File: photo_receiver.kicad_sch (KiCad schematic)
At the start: 7 parts

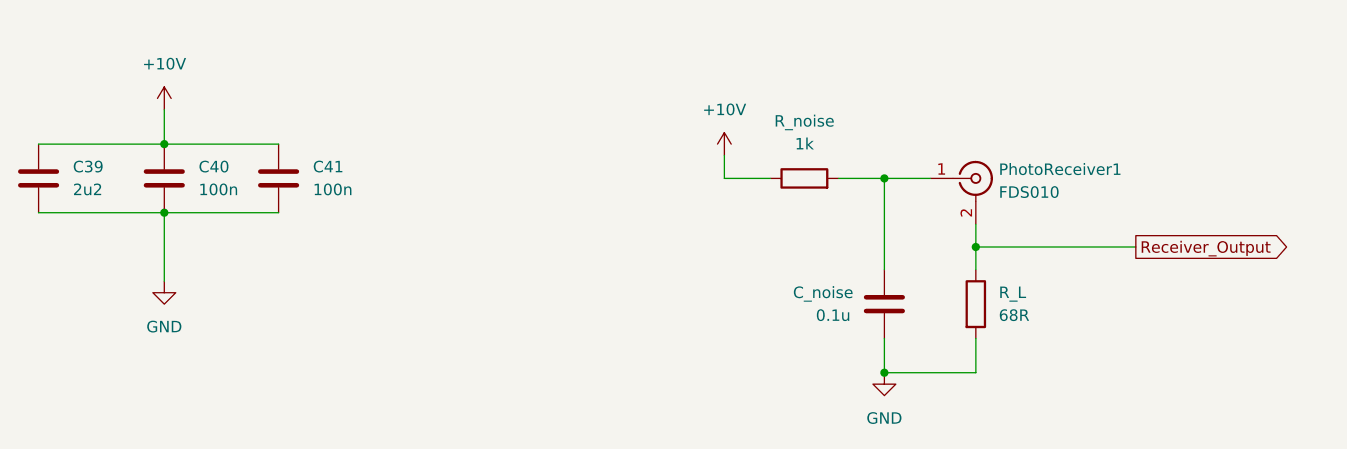
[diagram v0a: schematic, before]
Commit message: Resistor and cap footprints (except the ones the store cupboard doesn't have)
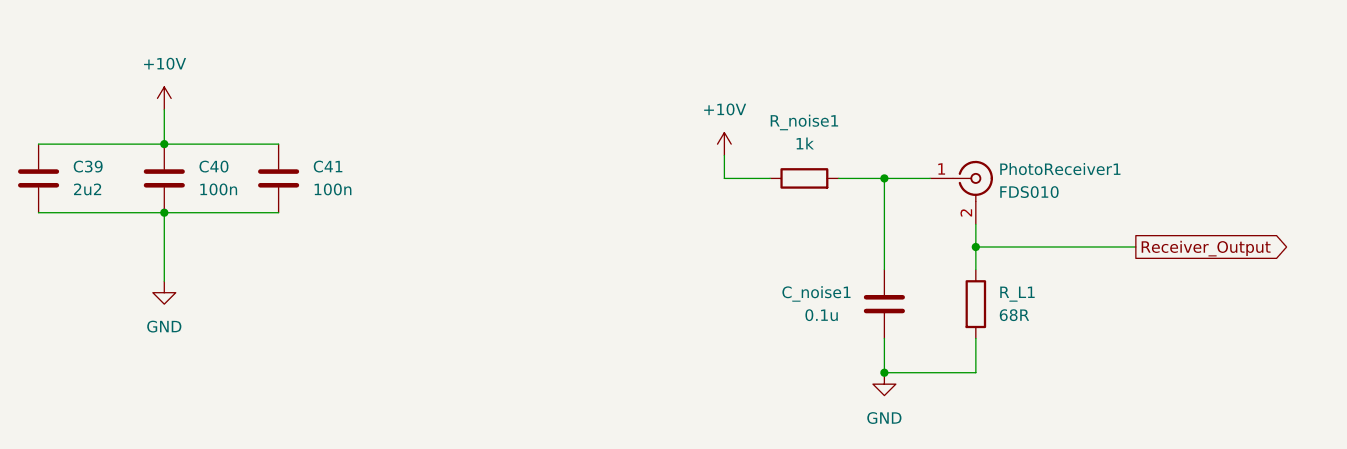
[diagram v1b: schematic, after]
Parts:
- C39: footprint (none) -> Capacitor_Tantalum_SMD:CP_EIA-3528-15_AVX-H_Pad1.50x2.35mm_HandSolder
- C40, C41: footprint (none) -> Capacitor_SMD:C_0805_2012Metric_Pad1.18x1.45mm_HandSolder
- C_noise1: renamed from C_noise; footprint (none) -> Capacitor_SMD:C_0805_2012Metric_Pad1.18x1.45mm_HandSolder
- R_L1: renamed from R_L; footprint (none) -> Resistor_SMD:R_0805_2012Metric_Pad1.20x1.40mm_HandSolder
- R_noise1: renamed from R_noise; footprint (none) -> Resistor_SMD:R_0805_2012Metric_Pad1.20x1.40mm_HandSolder
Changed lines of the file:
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@@
   (symbol (lib_id "Device:R") (at 123.19 91.44 90) (unit 1)
     (in_bom yes) (on_board yes) (fields_autoplaced)
-    (property "Reference" "R_noise" (id 0) (at 123.19 85.09 90))
+    (property "Reference" "R_noise1" (id 0) (at 123.19 85.09 90))
     (property "Value" "1k" (id 1) (at 123.19 87.63 90))
-    (property "Footprint" "" (id 2) (at 123.19 93.218 90)
+    (property "Footprint" "Resistor_SMD:R_0805_2012Metric_Pad1.20x1.40mm_HandSolder" (id 2) (at 123.19 93.218 90)
       (effects (font (size 1.27 1.27)) hide)
     )
@@
   (symbol (lib_id "Device:R") (at 142.24 105.41 0) (unit 1)
     (in_bom yes) (on_board yes) (fields_autoplaced)
-    (property "Reference" "R_L" (id 0) (at 144.78 104.1399 0)
+    (property "Reference" "R_L1" (id 0) (at 144.78 104.1399 0)
       (effects (font (size 1.27 1.27)) (justify left))
     )
@@
       (effects (font (size 1.27 1.27)) (justify left))
     )
-    (property "Footprint" "" (id 2) (at 140.462 105.41 90)
+    (property "Footprint" "Resistor_SMD:R_0805_2012Metric_Pad1.20x1.40mm_HandSolder" (id 2) (at 140.462 105.41 90)
       (effects (font (size 1.27 1.27)) hide)
     )
@@
       (effects (font (size 1.27 1.27)) (justify left))
     )
-    (property "Footprint" "" (id 2) (at 65.7352 95.25 0)
+    (property "Footprint" "Capacitor_SMD:C_0805_2012Metric_Pad1.18x1.45mm_HandSolder" (id 2) (at 65.7352 95.25 0)
       (effects (font (size 1.27 1.27)) hide)
     )
@@
   (symbol (lib_id "Device:C") (at 132.08 105.41 0) (unit 1)
     (in_bom yes) (on_board yes)
-    (property "Reference" "C_noise" (id 0) (at 121.92 104.14 0)
+    (property "Reference" "C_noise1" (id 0) (at 120.65 104.14 0)
       (effects (font (size 1.27 1.27)) (justify left))
     )
-    (property "Value" "0.1u" (id 1) (at 124.46 106.68 0)
+    (property "Value" "0.1u" (id 1) (at 123.19 106.68 0)
       (effects (font (size 1.27 1.27)) (justify left))
     )
-    (property "Footprint" "" (id 2) (at 133.0452 109.22 0)
+    (property "Footprint" "Capacitor_SMD:C_0805_2012Metric_Pad1.18x1.45mm_HandSolder" (id 2) (at 133.0452 109.22 0)
       (effects (font (size 1.27 1.27)) hide)
     )
@@
   (symbol (lib_id "power:GND") (at 132.08 113.03 0) (unit 1)
     (in_bom yes) (on_board yes) (fields_autoplaced)
-    (property "Reference" "#PWR?" (id 0) (at 132.08 119.38 0)
+    (property "Reference" "#PWR0108" (id 0) (at 132.08 119.38 0)
       (effects (font (size 1.27 1.27)) hide)
     )
@@
   (symbol (lib_id "power:+10V") (at 52.07 83.82 0) (unit 1)
     (in_bom yes) (on_board yes) (fields_autoplaced)
-    (property "Reference" "#PWR?" (id 0) (at 52.07 87.63 0)
+    (property "Reference" "#PWR0106" (id 0) (at 52.07 87.63 0)
       (effects (font (size 1.27 1.27)) hide)
     )
@@
       (effects (font (size 1.27 1.27)) (justify left))
     )
-    (property "Footprint" "" (id 2) (at 53.0352 95.25 0)
+    (property "Footprint" "Capacitor_SMD:C_0805_2012Metric_Pad1.18x1.45mm_HandSolder" (id 2) (at 53.0352 95.25 0)
       (effects (font (size 1.27 1.27)) hide)
     )
@@
   (symbol (lib_id "power:+10V") (at 114.3 88.9 0) (unit 1)
     (in_bom yes) (on_board yes) (fields_autoplaced)
-    (property "Reference" "#PWR?" (id 0) (at 114.3 92.71 0)
+    (property "Reference" "#PWR0107" (id 0) (at 114.3 92.71 0)
       (effects (font (size 1.27 1.27)) hide)
     )
@@
       (effects (font (size 1.27 1.27)) (justify left))
     )
-    (property "Footprint" "" (id 2) (at 39.0652 95.25 0)
+    (property "Footprint" "Capacitor_Tantalum_SMD:CP_EIA-3528-15_AVX-H_Pad1.50x2.35mm_HandSolder" (id 2) (at 39.0652 95.25 0)
       (effects (font (size 1.27 1.27)) hide)
     )

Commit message: added most of the sourcing info
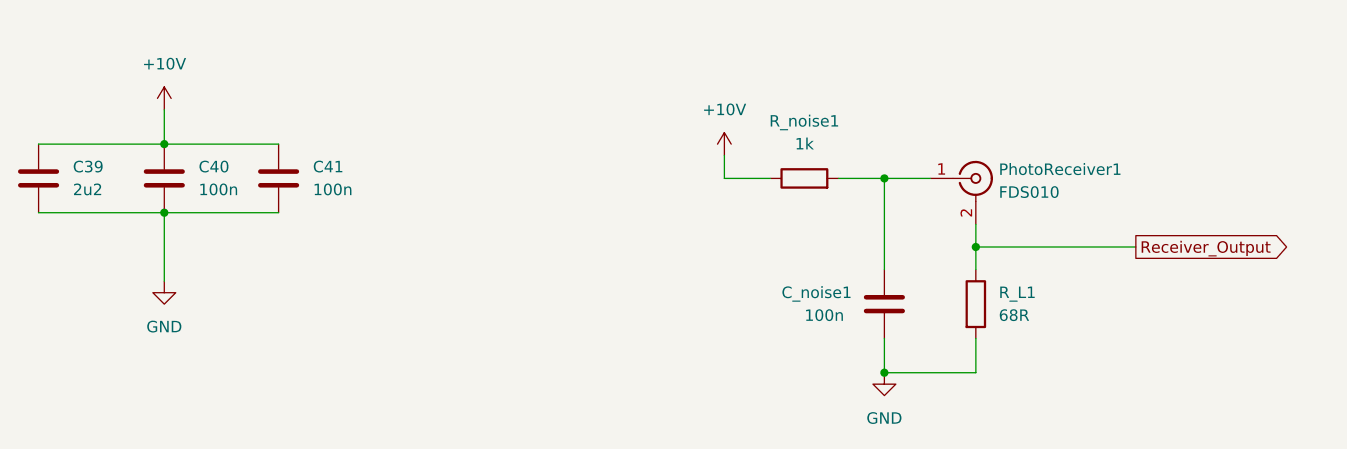
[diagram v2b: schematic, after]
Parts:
- C39, C40, C41, R_L1, R_noise1: Source (none) -> L3 store
- C_noise1: value 0.1u -> 100n; Source (none) -> L3 store
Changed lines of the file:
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@@
+      (effects (font (size 1.27 1.27)) hide)
+    )
+    (property "Source" "L3 store" (id 4) (at 123.19 91.44 0)
       (effects (font (size 1.27 1.27)) hide)
     )
@@
       (effects (font (size 1.27 1.27)) hide)
     )
+    (property "Source" "L3 store" (id 4) (at 142.24 105.41 0)
+      (effects (font (size 1.27 1.27)) hide)
+    )
     (pin "1")
     (pin "2")
@@
       (effects (font (size 1.27 1.27)) hide)
     )
+    (property "Source" "L3 store" (id 4) (at 64.77 91.44 0)
+      (effects (font (size 1.27 1.27)) hide)
+    )
     (pin "1")
     (pin "2")
@@
       (effects (font (size 1.27 1.27)) (justify left))
     )
-    (property "Value" "0.1u" (id 1) (at 123.19 106.68 0)
+    (property "Value" "100n" (id 1) (at 123.19 106.68 0)
       (effects (font (size 1.27 1.27)) (justify left))
     )
@@
     )
     (property "Datasheet" "~" (id 3) (at 132.08 105.41 0)
+      (effects (font (size 1.27 1.27)) hide)
+    )
+    (property "Source" "L3 store" (id 4) (at 132.08 105.41 0)
       (effects (font (size 1.27 1.27)) hide)
     )
@@
       (effects (font (size 1.27 1.27)) hide)
     )
+    (property "Source" "L3 store" (id 4) (at 52.07 91.44 0)
+      (effects (font (size 1.27 1.27)) hide)
+    )
     (pin "1")
     (pin "2")
@@
       (effects (font (size 1.27 1.27)) hide)
     )
+    (property "Source" "L3 store" (id 4) (at 38.1 91.44 0)
+      (effects (font (size 1.27 1.27)) hide)
+    )

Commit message: solved power drc problems
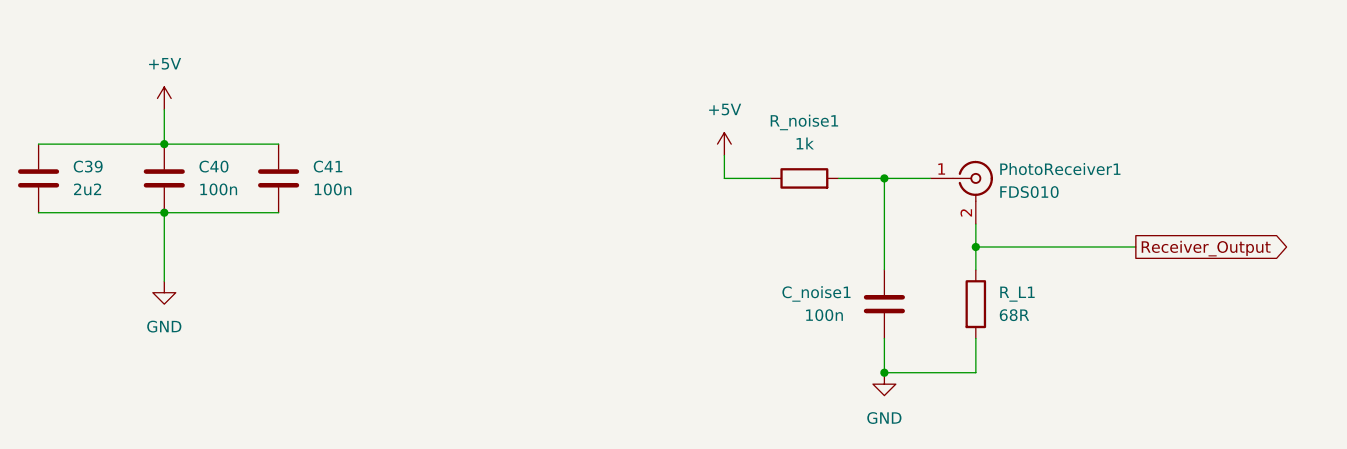
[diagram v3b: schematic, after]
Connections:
- net +10V renamed +5V
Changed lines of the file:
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@@
     (pin "2")
+  )
+  (symbol (lib_id "power:+5V") (at 114.3 88.9 0) (unit 1)
+    (in_bom yes) (on_board yes) (fields_autoplaced)
+    (property "Reference" "#PWR0107" (id 0) (at 114.3 92.71 0)
+      (effects (font (size 1.27 1.27)) hide)
+    )
+    (property "Value" "+5V" (id 1) (at 114.3 83.82 0))
+    (property "Footprint" "" (id 2) (at 114.3 88.9 0)
+      (effects (font (size 1.27 1.27)) hide)
+    )
+    (property "Datasheet" "" (id 3) (at 114.3 88.9 0)
+      (effects (font (size 1.27 1.27)) hide)
+    )
+    (pin "1")
   )
   (symbol (lib_id "Device:C") (at 132.08 105.41 0) (unit 1)
@@
     (pin "1")
   )
-  (symbol (lib_id "power:+10V") (at 52.07 83.82 0) (unit 1)
-    (in_bom yes) (on_board yes) (fields_autoplaced)
-    (property "Reference" "#PWR0106" (id 0) (at 52.07 87.63 0)
-      (effects (font (size 1.27 1.27)) hide)
-    )
-    (property "Value" "+10V" (id 1) (at 52.07 78.74 0))
-    (property "Footprint" "" (id 2) (at 52.07 83.82 0)
-      (effects (font (size 1.27 1.27)) hide)
-    )
-    (property "Datasheet" "" (id 3) (at 52.07 83.82 0)
-      (effects (font (size 1.27 1.27)) hide)
-    )
-    (pin "1")
-  )
   (symbol (lib_id "Device:C") (at 52.07 91.44 0) (unit 1)
     (in_bom yes) (on_board yes) (fields_autoplaced)
@@
     (pin "2")
   )
-  (symbol (lib_id "power:+10V") (at 114.3 88.9 0) (unit 1)
+  (symbol (lib_id "power:+5V") (at 52.07 83.82 0) (unit 1)
     (in_bom yes) (on_board yes) (fields_autoplaced)
-    (property "Reference" "#PWR0107" (id 0) (at 114.3 92.71 0)
+    (property "Reference" "#PWR0106" (id 0) (at 52.07 87.63 0)
       (effects (font (size 1.27 1.27)) hide)
     )
-    (property "Value" "+10V" (id 1) (at 114.3 83.82 0))
-    (property "Footprint" "" (id 2) (at 114.3 88.9 0)
+    (property "Value" "+5V" (id 1) (at 52.07 78.74 0))
+    (property "Footprint" "" (id 2) (at 52.07 83.82 0)
       (effects (font (size 1.27 1.27)) hide)
     )
-    (property "Datasheet" "" (id 3) (at 114.3 88.9 0)
+    (property "Datasheet" "" (id 3) (at 52.07 83.82 0)
       (effects (font (size 1.27 1.27)) hide)
     )

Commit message: Add SMA connector footprint and assign source
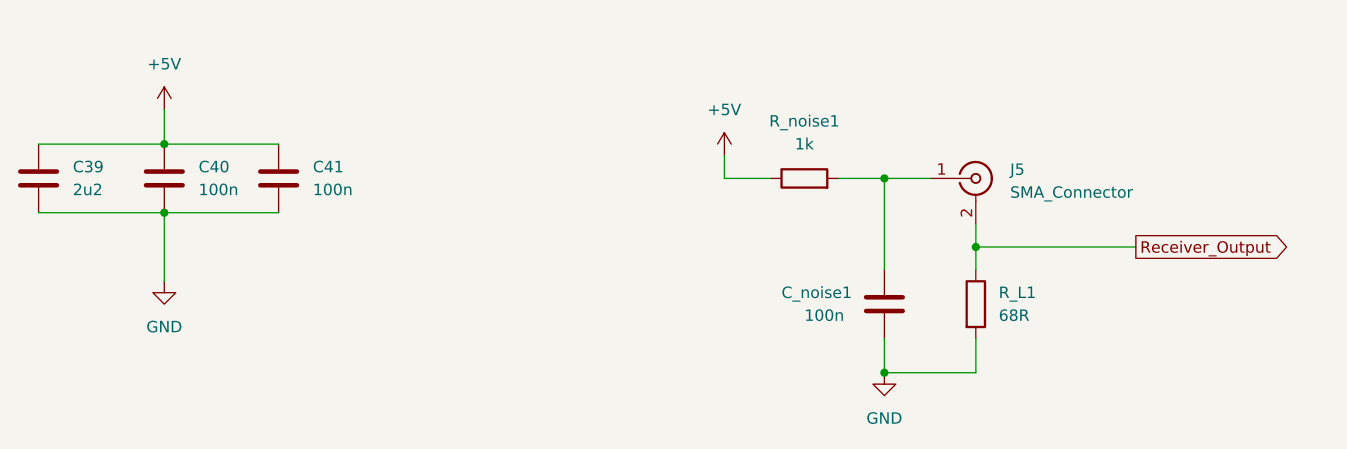
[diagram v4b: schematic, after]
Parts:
- J5: renamed from PhotoReceiver1; value FDS010 -> SMA_Connector; footprint Connector_Coaxial:SMA_Amphenol_901-144_Vertical -> SMA Connector:733910070; Source (none) -> https://onecall.farnell.com/molex/73391-0070/rf-coax-conn-s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
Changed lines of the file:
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@@
   (symbol (lib_id "Connector:Conn_Coaxial") (at 142.24 91.44 0) (unit 1)
     (in_bom yes) (on_board yes) (fields_autoplaced)
-    (property "Reference" "PhotoReceiver1" (id 0) (at 144.78 90.4631 0)
+    (property "Reference" "J5" (id 0) (at 146.05 90.4631 0)
       (effects (font (size 1.27 1.27)) (justify left))
     )
-    (property "Value" "FDS010" (id 1) (at 144.78 93.0031 0)
+    (property "Value" "SMA_Connector" (id 1) (at 146.05 93.0031 0)
       (effects (font (size 1.27 1.27)) (justify left))
     )
-    (property "Footprint" "Connector_Coaxial:SMA_Amphenol_901-144_Vertical" (id 2) (at 142.24 91.44 0)
+    (property "Footprint" "SMA Connector:733910070" (id 2) (at 142.24 91.44 0)
       (effects (font (size 1.27 1.27)) hide)
     )
@@
       (effects (font (size 1.27 1.27)) hide)
     )
+    (property "Source" "https://onecall.farnell.com/molex/73391-0070/rf-coax-conn-sma-jack-50-ohm-pcb/dp/1909301" (id 4) (at 142.24 91.44 0)
+      (effects (font (size 1.27 1.27)) hide)
+    )

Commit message: Change SMA connector symbol to match footprint
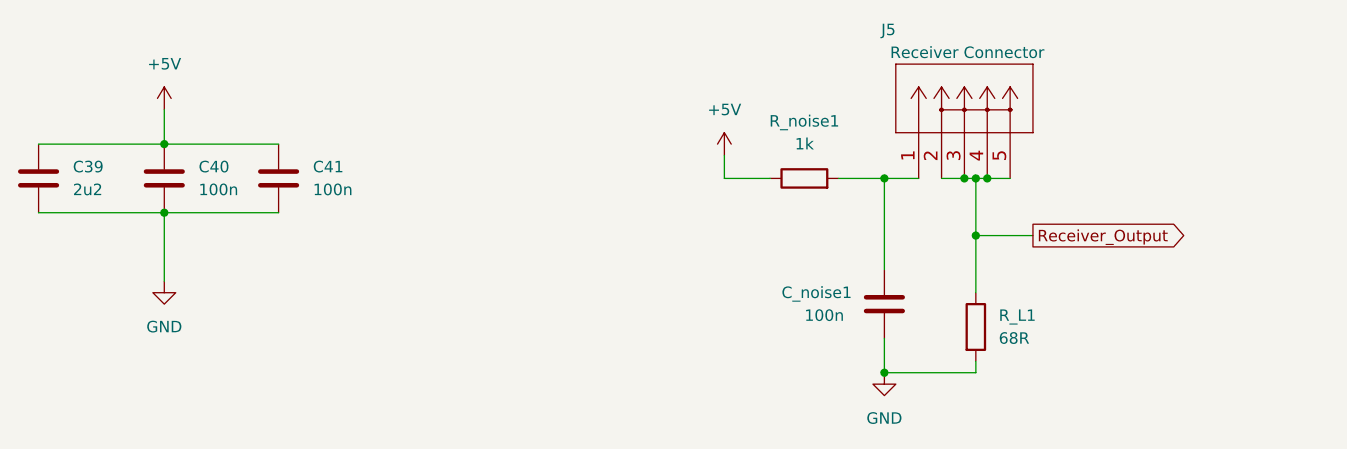
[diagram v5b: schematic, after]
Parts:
- J5: value SMA_Connector -> Receiver Connector; footprint SMA Connector:733910070 -> CONN_73391-0070_MOL; symbol Connector:Conn_Coaxial -> SMA_Connector:733910070
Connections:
- net Receiver_Output: now also J5.3, J5.4, J5.5
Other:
- moved on the sheet: R_L1
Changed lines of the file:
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@@
   (junction (at 52.07 95.25) (diameter 0) (color 0 0 0 0)
   )
-  (junction (at 142.24 99.06) (diameter 0) (color 0 0 0 0)
+  (junction (at 142.24 97.79) (diameter 0) (color 0 0 0 0)
+  )
+  (junction (at 140.97 91.44) (diameter 0) (color 0 0 0 0)
+  )
+  (junction (at 142.24 91.44) (diameter 0) (color 0 0 0 0)
   )
   (junction (at 132.08 91.44) (diameter 0) (color 0 0 0 0)
+  )
+  (junction (at 143.51 91.44) (diameter 0) (color 0 0 0 0)
   )
   (wire (pts (xy 132.08 109.22) (xy 132.08 113.03))
     (stroke (width 0) (type default) (color 0 0 0 0))
   )
-  (wire (pts (xy 142.24 96.52) (xy 142.24 99.06))
+  (wire (pts (xy 142.24 91.44) (xy 142.24 97.79))
     (stroke (width 0) (type default) (color 0 0 0 0))
   )
-  (wire (pts (xy 142.24 99.06) (xy 142.24 101.6))
-    (stroke (width 0) (type default) (color 0 0 0 0))
-  )
-  (wire (pts (xy 142.24 99.06) (xy 160.02 99.06))
+  (wire (pts (xy 142.24 91.44) (xy 143.51 91.44))
     (stroke (width 0) (type default) (color 0 0 0 0))
   )
@@
     (stroke (width 0) (type default) (color 0 0 0 0))
   )
-  (wire (pts (xy 132.08 91.44) (xy 137.16 91.44))
+  (wire (pts (xy 142.24 97.79) (xy 142.24 104.14))
+    (stroke (width 0) (type default) (color 0 0 0 0))
+  )
+  (wire (pts (xy 132.08 91.44) (xy 135.89 91.44))
     (stroke (width 0) (type default) (color 0 0 0 0))
   )
@@
     (stroke (width 0) (type default) (color 0 0 0 0))
   )
-  (wire (pts (xy 142.24 109.22) (xy 142.24 113.03))
+  (wire (pts (xy 142.24 111.76) (xy 142.24 113.03))
     (stroke (width 0) (type default) (color 0 0 0 0))
   )
@@
     (stroke (width 0) (type default) (color 0 0 0 0))
   )
+  (wire (pts (xy 142.24 97.79) (xy 148.59 97.79))
+    (stroke (width 0) (type default) (color 0 0 0 0))
+  )
   (wire (pts (xy 38.1 87.63) (xy 52.07 87.63))
+    (stroke (width 0) (type default) (color 0 0 0 0))
+  )
+  (wire (pts (xy 143.51 91.44) (xy 146.05 91.44))
     (stroke (width 0) (type default) (color 0 0 0 0))
   )
@@
     (stroke (width 0) (type default) (color 0 0 0 0))
   )
-  (global_label "Receiver_Output" (shape output) (at 160.02 99.06 0) (fields_autoplaced)
+  (wire (pts (xy 140.97 91.44) (xy 142.24 91.44))
+    (stroke (width 0) (type default) (color 0 0 0 0))
+  )
+  (wire (pts (xy 138.43 91.44) (xy 140.97 91.44))
+    (stroke (width 0) (type default) (color 0 0 0 0))
+  )
+  (global_label "Receiver_Output" (shape output) (at 148.59 97.79 0) (fields_autoplaced)
     (effects (font (size 1.27 1.27)) (justify left))
-    (property "Intersheet References" "${INTERSHEET_REFS}" (id 0) (at 177.6126 98.9806 0)
+    (property "Intersheet References" "${INTERSHEET_REFS}" (id 0) (at 166.1826 97.7106 0)
       (effects (font (size 1.27 1.27)) (justify left) hide)
     )
@@
     (pin "2")
   )
-  (symbol (lib_id "Device:R") (at 142.24 105.41 0) (unit 1)
+  (symbol (lib_id "Device:R") (at 142.24 107.95 0) (unit 1)
     (in_bom yes) (on_board yes) (fields_autoplaced)
-    (property "Reference" "R_L1" (id 0) (at 144.78 104.1399 0)
+    (property "Reference" "R_L1" (id 0) (at 144.78 106.6799 0)
       (effects (font (size 1.27 1.27)) (justify left))
     )
-    (property "Value" "68R" (id 1) (at 144.78 106.6799 0)
+    (property "Value" "68R" (id 1) (at 144.78 109.2199 0)
       (effects (font (size 1.27 1.27)) (justify left))
     )
-    (property "Footprint" "Resistor_SMD:R_0805_2012Metric_Pad1.20x1.40mm_HandSolder" (id 2) (at 140.462 105.41 90)
+    (property "Footprint" "Resistor_SMD:R_0805_2012Metric_Pad1.20x1.40mm_HandSolder" (id 2) (at 140.462 107.95 90)
       (effects (font (size 1.27 1.27)) hide)
     )
-    (property "Datasheet" "~" (id 3) (at 142.24 105.41 0)
+    (property "Datasheet" "~" (id 3) (at 142.24 107.95 0)
       (effects (font (size 1.27 1.27)) hide)
     )
-    (property "Source" "L3 store" (id 4) (at 142.24 105.41 0)
+    (property "Source" "L3 store" (id 4) (at 142.24 107.95 0)
       (effects (font (size 1.27 1.27)) hide)
     )
@@
     (pin "2")
   )
-  (symbol (lib_id "Connector:Conn_Coaxial") (at 142.24 91.44 0) (unit 1)
-    (in_bom yes) (on_board yes) (fields_autoplaced)
-    (property "Reference" "J5" (id 0) (at 146.05 90.4631 0)
+  (symbol (lib_id "SMA_Connector:733910070") (at 135.89 91.44 90) (unit 1)
+    (in_bom yes) (on_board yes)
+    (property "Reference" "J5" (id 0) (at 133.35 74.93 90)
       (effects (font (size 1.27 1.27)) (justify left))
     )
-    (property "Value" "SMA_Connector" (id 1) (at 146.05 93.0031 0)
+    (property "Value" "Receiver Connector" (id 1) (at 149.86 77.47 90)
       (effects (font (size 1.27 1.27)) (justify left))
     )
-    (property "Footprint" "SMA Connector:733910070" (id 2) (at 142.24 91.44 0)
+    (property "Footprint" "CONN_73391-0070_MOL" (id 2) (at 142.494 81.28 0)
+      (effects (font (size 1.524 1.524)) hide)
+    )
+    (property "Datasheet" " ~" (id 3) (at 135.89 91.44 0)
       (effects (font (size 1.27 1.27)) hide)
     )
-    (property "Datasheet" " ~" (id 3) (at 142.24 91.44 0)
-      (effects (font (size 1.27 1.27)) hide)
-    )
-    (property "Source" "https://onecall.farnell.com/molex/73391-0070/rf-coax-conn-sma-jack-50-ohm-pcb/dp/1909301" (id 4) (at 142.24 91.44 0)
+    (property "Source" "https://onecall.farnell.com/molex/73391-0070/rf-coax-conn-sma-jack-50-ohm-pcb/dp/1909301" (id 4) (at 135.89 91.44 0)
       (effects (font (size 1.27 1.27)) hide)
     )
     (pin "1")
     (pin "2")
+    (pin "3")
+    (pin "4")
+    (pin "5")
   )
   (symbol (lib_id "power:GND") (at 132.08 113.03 0) (unit 1)
